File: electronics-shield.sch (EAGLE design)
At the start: 0 parts

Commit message: H-Bridge change from L298P to TLE9201S, better wiring
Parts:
- added C1, C11, C12, C13, C14, C19, C2, C20, C21, C22, C23, C3, C4, C6, C9: 100n, resistor:C-EUC0603K
- added C10: 1u, resistor:C-EUC0603K
- added C15: 4.7uF, resistor:C-EUC0603K
- added C16: 1uF, resistor:C-EUC0603K
- added C17: 100u, resistor:CPOL-EU153CLV-0807
- added C18: 22u, resistor:C-EUC0603K
- added C24: 0.1uF, rcl:C-EUC0603
- added C5: 4u7, resistor:C-EUC0603K
- added C7, C8: 20p, resistor:C-EUC0603K
- added D1, D10, D11, D12, D13, D14, D15, D16, D2, D3, D4, D5, D6, D7, D8, D9: SK38SMA, diode:DIODE-SOD123
- added D17: SMBJ5.0A-TR, diode:SUPPRESSOR-SMBJ
- added F1, F2, F3: SL125-33, polyfuse-smd_10:2920L050
- added IC1: MCP1703CB, linear:MCP1703CB
- added JP1: Listwa kołkowa 2.54mm prosta 1x2 (2pin), pinhead:PINHD-1X2
- added JP10: gniazdo IDC męskie 6pin proste, con-harting-ml:ML6
- added JP2, JP3, JP4: Listwa kołkowa 2.54mm prosta 1x3 (3pin), Synergiczne:PINHD-1X3STRAIGHT
- added JP5: Listwa stykowa 2.54mm prosta 2x20 (40-pin), wydłużona, RASPBERRY_PI_Bplus-eagle5:RASPBERRY_PI_B+_TPLACE
- added JP6: gniazdo IDC męskie 10pin proste, con-3m:2510-
- added JP7: gniazdo IDC męskie 8pin proste, Simplex-Connectors:2508-
- added JP8: Listwa zaciskowa rozłączalna 3.81mm 2pin kątowe 90° gniazdo, con-phoenix-381_l:MC2
- added JP9: Listwa zaciskowa rozłączalna 3.50mm 8pin kątowe 90° gniazdo, con-phoenix-350:1751303
- added PCB1, PCB2, PCB3: Moduł przetwornicy DC-DC Step-down 4.5..28V --- regulowane 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, Kell Ideas:MP1584
- added Q1: 8 MHz, crystal:CRYSTALHC49UP
- added Q2: MOSFET-PCHANNELSMD, User-Submitted:MOSFET-PCHANNELSMD
- added R1, R2, R3, R4: 10k, rcl:R-EU_R0603
- added R10: 100k, rcl:R-EU_R0603
- added R11, R13, R14, R5, R8, R9: 10k, resistor:R-EU_R0603
- added R12: 1k, resistor:R-EU_R0603
- added R6, R7: 4k7, resistor:R-EU_R0603
- added SJ1: Zworka cynowa, jumper:SJ2W
- added U1, U2, U3, U4: TLE9201SGAUMA1, Kell Ideas:TLE9201SGAUMA1
- added U5: STM32F051C8T, STM32F030:STM32F051C8T
- added U6, U7: SN74LVC4245APWR, Texas Instruments_By_element14_Batch_1:SN74LVC4245APWR
- added U8: 24LC256, SparkFun-IC-Memory:EEPROM-I2CSMD
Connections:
- new net +3V3: C10.1, C11.1, C19.1, C20.1, C24.1, C5.1, C6.1, C9.1, JP10.4, R5.2, R6.2, R7.2, R8.2, SJ1.2, U5PWR.VDD, U5PWR.VDDA, U6.VCCB_(3.3_V), U6.VCCB_(3.3_V)_2, U7.VCCB_(3.3_V), U7.VCCB_(3.3_V)_2, U8.VCC, U8.WP
- new net +5V: C1.1, C15.1, C2.1, C21.1, C22.1, C23.1, C3.1, C4.1, D17.C, IC1.VI, JP5.5V0@1, JP5.5V0@2, JP6-3.KL, JP7-2.KL, Q2.S, U1.VSO, U2.VSO, U3.VSO, U4.VSO, U6.(5_V)_VCCA, U7.(5_V)_VCCA
- new net +5V_RAW: F1.2, PCB1.VOUT+
- new net +7V/1: C13.1, F2.1, JP4.2, JP6-1.KL
- new net +7V/1_RAW: F2.2, PCB2.VOUT+
- new net +7V/2: C14.1, F3.2, JP2.2, JP3.2, JP6-2.KL
- new net +7V/2_RAW: F3.1, PCB3.VOUT+
- new net 3V3_RPI: JP5.3V3@1, SJ1.3
- new net 3V3_STABILIZED: C16.1, IC1.VO, SJ1.1
- new net 5V_NOT_TRIMMED: C12.1, F1.1, Q2.D
- new net BAT_MEAS: C18.1, R11.1, R12.2, U5PA.PA4
- new net BOOT0: R9.2, U5CTL.BOOT0
- new net D1-R3: D17.A, Q2.G, R10.2
- new net DATA_N: JP1.2, JP7-3.KL
- new net DATA_P: JP1.1, JP7-4.KL
- new net EN1: U1.PWM, U6.A1
- new net EN1_UC: U5PA.PA6, U6.B1
- new net EN2: U3.PWM, U6.A2
- new net EN2_UC: U5PA.PA7, U6.B2
- new net EN3: U2.PWM, U6.A3
- new net EN3_UC: U5PB.PB0, U6.B3
- new net EN4: U4.PWM, U6.A4
- new net EN4_UC: U5PB.PB1, U6.B4
- new net GND: C1.2, C10.2, C11.2, C12.2, C13.2, C14.2, C15.2, C16.2, C17.-, C18.2, C19.2, C2.2, C20.2, C21.2, C22.2, C23.2, C24.2, C3.2, C4.2, C5.2, C6.2, C7.1, C8.1, C9.2, D10.A, D11.A, D12.A, D13.A, D14.A, D15.A, D16.A, D9.A, IC1.GND, JP10.3, JP2.3, JP3.3, JP4.3, JP5.GND@1, JP5.GND@2, JP5.GND@3, JP5.GND@4, JP5.GND@5, JP5.GND@6, JP5.GND@7, JP5.GND@8, JP6-10.KL, JP6-9.KL, JP7-1.KL, JP7-8.KL, JP8.1.SK, PCB1.VIN-, PCB1.VOUT-, PCB2.VIN-, PCB2.VOUT-, PCB3.VIN-, PCB3.VOUT-, R1.1, R10.1, R12.1, R13.2, R14.2, R2.1, R3.1, R4.1, R9.1, U1.GND@1, U1.GND@2, U2.GND@1, U2.GND@2, U3.GND@1, U3.GND@2, U4.GND@1, U4.GND@2, U5PWR.VSS, U5PWR.VSSA, U6.GND, U6.GND_2, U6.GND_3, U7.GND, U7.GND_2, U7.GND_3, U8.A1, U8.A2, U8.VSS
- new net IN11: U1.DIR, U6.A5
- new net IN11_UC: U5PB.PB8, U6.B5
- new net IN12: U6.A6
- new net IN12_UC: U6.B6
- new net IN21: U3.DIR, U6.A7
- new net IN21_UC: U5PA.PA11, U6.B7
- new net IN22: U6.A8
- new net IN22_UC: U6.B8
- new net IN31: U2.DIR, U7.A1
- new net IN31_UC: U5PB.PB12, U7.B1
- new net IN32: U7.A2
- new net IN32_UC: U7.B2
- new net IN41: U4.DIR, U7.A3
- new net IN41_UC: U5PB.PB14, U7.B3
- new net IN42: U7.A4
- new net IN42_UC: U7.B4
- new net LED: U5PA.PA5
- new net MOT11: D16.C, D8.A, JP9-7.K, U1.OUT1
- new net MOT12: D15.C, D7.A, JP9-8.K, U1.OUT2
- new net MOT21: D14.C, D6.A, JP9-5.K, U3.OUT1
- new net MOT22: D13.C, D5.A, JP9-6.K, U3.OUT2
- new net MOT31: D12.C, D4.A, JP9-3.K, U2.OUT1
- new net MOT32: D11.C, D3.A, JP9-4.K, U2.OUT2
- new net MOT41: D10.C, D2.A, JP9-1.K, U4.OUT1
- new net MOT42: D1.A, D9.C, JP9-2.K, U4.OUT2
- new net N$1: R13.1, U6.DIR, U6.~OE
- new net N$2: R14.1, U7.DIR, U7.~OE
- new net N$3: U7.A8
- new net N$4: U7.B8
- new net N$8: JP10.6
- new net NRST: JP10.5, JP5.GPIO18, R8.1, U5CTL.NRST
- new net OSCILATOR_N: C7.2, Q1.2, U5CTL.PF0-OSC_IN
- new net OSCILATOR_P: C8.2, Q1.1, U5CTL.PF1-OSC_OUT
- new net RPI_CLK: JP5.GPIO11/SCLK, JP7-7.KL, U5PB.PB3
- new net RPI_MISO: JP5.GPIO09/MISO, JP7-5.KL, U5PB.PB4
- new net RPI_MOSI: JP5.GPIO10/MOSI, JP7-6.KL, U5PB.PB5
- new net RPI_RXD: JP5.RXD0/GPIO15, U5PB.PB6
- new net RPI_TXD: JP5.TXD0/GPIO14, U5PB.PB7
- new net SCL: JP5.GPIO03/SCL1, R7.1, U5PA.PF6, U8.SCL
- new net SCL_TX: JP6-5.KL, U5PB.PB10
- new net SDA: JP5.GPIO02/SDA1, R6.1, U5PA.PF7, U8.SDA
- new net SDA_RX: JP6-4.KL, U5PB.PB11
- new net SEN1: U5PA.PA0
- new net SEN2: U5PA.PA1
- new net SEN3: U5PA.PA2
- new net SEN4: U5PA.PA3
- new net SERVO1: JP2.1, JP6-6.KL, U7.A5
- new net SERVO1_UC: U5PA.PA8, U7.B5
- new net SERVO2: JP3.1, JP6-7.KL, U7.A6
- new net SERVO2_UC: U5PA.PA9, U7.B6
- new net SERVO3: JP4.1, JP6-8.KL, U7.A7
- new net SERVO3_UC: U5PA.PA10, U7.B7
- new net SPI1_NSS: JP5.!CE0!/GPIO08, R5.1, U5PA.PA15
- new net SWCLK: JP10.1, JP5.GEN6/GPIO25, U5PA.PA14-SWCLK
- new net SWDIO: JP10.2, JP5.GEN5/GPIO24, U5PA.PA13-SWDIO
- new net U5_DIS: R1.2, U1.DIS
- new net U6_DIS: R2.2, U2.DIS
- new net U7_DIS: R3.2, U3.DIS
- new net U8_DIS: R4.2, U4.DIS
- new net VCC: C17.+, D1.C, D2.C, D3.C, D4.C, D5.C, D6.C, D7.C, D8.C, JP8.2.SK, PCB1.VIN+, PCB2.VIN+, PCB3.VIN+, R11.2, U1.VS, U2.VS, U3.VS, U4.VS
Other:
- note added: "B to A"
- note added: "Battery Measurement"
- note added: "I2C2"
- note added: "MOTOR CONTROLLERS"
- note added: "Manipulator + USB"
- note added: "NC"
- note added: "Power Supply Raspberry 5V / 3A"
- note added: "Power Supply Servo 7V / 3 A"
- note added: "RPI HEADER"
- note added: "Second Servo PS 7V / 3 A"

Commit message: changed base for 7.c
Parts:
- removed C21, C22, C23: 100n, resistor:C-EUC0603K
- removed C24: 0.1uF, rcl:C-EUC0603
- removed JP10: gniazdo IDC męskie 6pin proste, con-harting-ml:ML6
- removed JP4: Listwa kołkowa 2.54mm prosta 1x3 (3pin), Synergiczne:PINHD-1X3STRAIGHT
- removed JP5: Listwa stykowa 2.54mm prosta 2x20 (40-pin), wydłużona, RASPBERRY_PI_Bplus-eagle5:RASPBERRY_PI_B+_TPLACE
- removed JP6: gniazdo IDC męskie 10pin proste, con-3m:2510-
- removed JP7: gniazdo IDC męskie 8pin proste, Simplex-Connectors:2508-
- removed JP8: Listwa zaciskowa rozłączalna 3.81mm 2pin kątowe 90° gniazdo, con-phoenix-381_l:MC2
- removed JP9: Listwa zaciskowa rozłączalna 3.50mm 8pin kątowe 90° gniazdo, con-phoenix-350:1751303
- removed PCB2, PCB3: Moduł przetwornicy DC-DC Step-down 4.5..28V --- regulowane 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, Kell Ideas:MP1584
- removed R14: 10k, resistor:R-EU_R0603
- removed U3, U4: TLE9201SGAUMA1, Kell Ideas:TLE9201SGAUMA1
- removed U5: STM32F051C8T, STM32F030:STM32F051C8T
- removed U6, U7: SN74LVC4245APWR, Texas Instruments_By_element14_Batch_1:SN74LVC4245APWR
- removed U8: 24LC256, SparkFun-IC-Memory:EEPROM-I2CSMD
- added $3_0_$_2018-08-14_21-12-08, $3_1_$_2018-08-14_21-12-08, $3_2_$_2018-08-14_21-12-08: Moduł przetwornicy DC-DC Step-down 4.5..28V --- regulowane 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, Kell Ideas:MP1584_MODULE
- added IC2, IC3, IC4: TLE9201SG, Kell Ideas:TLE9201SG
- added IC5: LINEAR_MCP1703CB, electronics-shield:LINEAR_MCP1703CB
- added J1: USB-MICRO-B, Kell Ideas:USB-MICRO-B
- added LED1, LED2, LED3, LED4, LED5: LEDCHIPLED_0603, audio amplifier example:LEDCHIPLED_0603
- added Q3: ON-SEMICONDUCTOR---NTZD3154NT1G_ON_SEMICONDUCTOR_NTZD3154NT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, electronics-shield:ON-SEMICONDUCTOR---NTZD3154NT1G_ON_SEMICONDUCTOR_NTZD3154NT1GON_SEMICONDUCTOR_NTZD3154NT1G_0_0
- added RN1, RN2: 1k, SparkFun-Resistors:1KOHM-ARRAY(4)-0805_ARV-1/10W-5%
- added SJ2: (no value), Kell Ideas:SOLDER_JUMPER
- added SV1: gniazdo IDC męskie 6pin proste, Kell Ideas:ML6
- added SV2: (no value), Kell Ideas:ML10
- added SV3: ML8, Kell Ideas:ML8
- added X1: CONNECTOR_PHOENIX_3.81, Kell Ideas:CONNECTOR_PHOENIX_3.81
- added X2: Listwa zaciskowa rozłączalna 3.50mm 8pin kątowe 90° gniazdo, Kell Ideas:CONNECTOR_PHOENIX
- added Y1: 8 MHz, Kell Ideas:CRYSTAL
- C1, C10, C11, C12, C13, C14, C15, C16, C18, C19, C2, C3, C4, C5, C6, C7, C8, C9: device resistor:C-EUC0603K -> Kell Ideas:CAPACITOR_SMD
- C17: device resistor:CPOL-EU153CLV-0807 -> Kell Ideas:CAPACITOR_POL_SMD
- C20: value 100n -> 0.1uF; device resistor:C-EUC0603K -> Kell Ideas:CAPACITOR_SMD
- D1, D10, D11, D12, D13, D14, D15, D16, D2, D3, D4, D5, D6, D7, D8, D9: device diode:DIODE-SOD123 -> Kell Ideas:DIODE_SMD
- D17: device diode:SUPPRESSOR-SMBJ -> Kell Ideas:SUPPRESSOR-SMBJ
- F1, F2, F3: device polyfuse-smd_10:2920L050 -> Kell Ideas:PPTCD
- IC1: value MCP1703CB -> TLE9201SG; device linear:MCP1703CB -> Kell Ideas:TLE9201SG
- JP1: value Listwa kołkowa 2.54mm prosta 1x2 (2pin) -> Listwa kołkowa 2.54mm prosta 1x3 (3pin); device pinhead:PINHD-1X2 -> Kell Ideas:PINHD-1X3_DNP
- JP2, JP3: device Synergiczne:PINHD-1X3STRAIGHT -> Kell Ideas:PINHD-1X3_DNP
- PCB1: value Moduł przetwornicy DC-DC Step-down 4.5..28V --- regulowane 0.8..20V MP1584 -> Listwa stykowa 2.54mm prosta 2x20 (40-pin), wydłużona; device Kell Ideas:MP1584 -> Kell Ideas:RASPBERRY_PI_B+_TPLACE
- Q1: value 8 MHz -> USER-SUBMITTED_MOSFET-PCHANNELSMD; device crystal:CRYSTALHC49UP -> electronics-shield:USER-SUBMITTED_MOSFET-PCHANNELSMD; LINK YIC 49SLMT 8.00MHZ 20PF 30PPM -> (none)
- Q2: value MOSFET-PCHANNELSMD -> ON-SEMICONDUCTOR---NTZD3154NT1G_ON_SEMICONDUCTOR_NTZD3154NT1GON_SEMICONDUCTOR_NTZD3154NT1G_0_0; device User-Submitted:MOSFET-PCHANNELSMD -> electronics-shield:ON-SEMICONDUCTOR---NTZD3154NT1G_ON_SEMICONDUCTOR_NTZD3154NT1GON_SEMICONDUCTOR_NTZD3154NT1G_0_0
- R1, R4: device rcl:R-EU_R0603 -> Kell Ideas:RESISTOR_SMD
- R10: value 100k -> 330; device rcl:R-EU_R0603 -> Kell Ideas:RESISTOR_SMD
- R11: value 10k -> 330; device resistor:R-EU_R0603 -> Kell Ideas:RESISTOR_SMD
- R12: value 1k -> 200; device resistor:R-EU_R0603 -> Kell Ideas:RESISTOR_SMD
- R13: value 10k -> 200; device resistor:R-EU_R0603 -> Kell Ideas:RESISTOR_SMD
- R2, R3: value 10k -> 4k7; device rcl:R-EU_R0603 -> Kell Ideas:RESISTOR_SMD
- R5: device resistor:R-EU_R0603 -> Kell Ideas:RESISTOR_SMD
- R6: value 4k7 -> 100k; device resistor:R-EU_R0603 -> Kell Ideas:RESISTOR_SMD
- R7: value 4k7 -> 10k; device resistor:R-EU_R0603 -> Kell Ideas:RESISTOR_SMD
- R8: value 10k -> 1k; device resistor:R-EU_R0603 -> Kell Ideas:RESISTOR_SMD
- R9: value 10k -> 1.5k; device resistor:R-EU_R0603 -> Kell Ideas:RESISTOR_SMD
- SJ1: value Zworka cynowa -> (none); device jumper:SJ2W -> Kell Ideas:SOLDER_JUMPER
- U1: value TLE9201SGAUMA1 -> STM32F0XX8T; device Kell Ideas:TLE9201SGAUMA1 -> Kell Ideas:STM32F0XX8T
- U2: value TLE9201SGAUMA1 -> EEPROM-I2C; device Kell Ideas:TLE9201SGAUMA1 -> Kell Ideas:EEPROM-I2C
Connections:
- removed net EN1_UC: U5PA.PA6, U6.B1
- removed net EN2_UC: U5PA.PA7, U6.B2
- removed net EN3_UC: U5PB.PB0, U6.B3
- removed net EN4_UC: U5PB.PB1, U6.B4
- removed net IN11_UC: U5PB.PB8, U6.B5
- removed net IN12: U6.A6
- removed net IN12_UC: U6.B6
- removed net IN21_UC: U5PA.PA11, U6.B7
- removed net IN22: U6.A8
- removed net IN22_UC: U6.B8
- removed net IN31_UC: U5PB.PB12, U7.B1
- removed net IN32: U7.A2
- removed net IN32_UC: U7.B2
- removed net IN41_UC: U5PB.PB14, U7.B3
- removed net IN42: U7.A4
- removed net IN42_UC: U7.B4
- removed net U5_DIS: R1.2, U1.DIS
- removed net U6_DIS: R2.2, U2.DIS
- removed net U7_DIS: R3.2, U3.DIS
- removed net U8_DIS: R4.2, U4.DIS
- new net N$14: Q2B.S2, RN2C.1
- new net N$16: Q2B.D2, RN2D.1
- new net N$5: LED5.C, R13.1
- new net SO1-SI3: IC1.SO, IC3.SI
- new net SO2-SI4: IC2.SO, IC4.SI
- new net SO3-SI2: IC2.SI, IC3.SO
- new net TLE_NSS: IC1.CS_N, IC2.CS_N, IC3.CS_N, IC4.CS_N, U1PB.PB2
- net +3V3: now also C1.1, C2.1, C3.1, C4.1, IC1.VSO, IC2.VSO, IC3.VSO, IC4.VSO, LED5.A, Q2A.G1, Q2B.G2, Q3A.G1, Q3B.G2, R1.2, R2.2, R3.2, R4.2, RN1A.2, RN1C.2, RN2A.2, RN2C.2, SJ1.1, SJ2.1, SV1.4, U1PWR.VDD, U1PWR.VDDA, U2.VCC, U2.WP; no longer C19.1, C24.1, JP10.4, R5.2, R6.2, R7.2, R8.2, SJ1.2, U5PWR.VDD, U5PWR.VDDA, U6.VCCB_(3.3_V), U6.VCCB_(3.3_V)_2, U7.VCCB_(3.3_V), U7.VCCB_(3.3_V)_2, U8.VCC, U8.WP
- net +5V: now also C19.1, IC5.VI, LED4.A, PCB1.5V0@1, PCB1.5V0@2, Q1.S, RN1B.2, RN1D.2, RN2B.2, RN2D.2, SV2.3, SV3.P$2; no longer C1.1, C2.1, C21.1, C22.1, C23.1, C3.1, C4.1, IC1.VI, JP5.5V0@1, JP5.5V0@2, JP6-3.KL, JP7-2.KL, Q2.S, U1.VSO, U2.VSO, U3.VSO, U4.VSO, U6.(5_V)_VCCA, U7.(5_V)_VCCA
- net +5V_RAW: now also $3_0_$_2018-08-14_21-12-08.VOUT+; no longer PCB1.VOUT+
- net +7V/1: now also JP3.2, LED2.A, SV2.1; no longer JP4.2, JP6-1.KL
- net +7V/1_RAW: now also $3_1_$_2018-08-14_21-12-08.VOUT+; no longer PCB2.VOUT+
- net +7V/2: now also JP1.2, LED3.A, SV2.2; no longer JP3.2, JP6-2.KL
- net +7V/2_RAW: now also $3_2_$_2018-08-14_21-12-08.VOUT+; no longer PCB3.VOUT+
- net 3V3_RPI: now also PCB1.3V3@1, SJ2.2; no longer JP5.3V3@1, SJ1.3
- net 3V3_STABILIZED: now also IC5.VO, SJ1.2; no longer IC1.VO, SJ1.1
- net 5V_NOT_TRIMMED: now also Q1.D; no longer Q2.D
- net BAT_MEAS: now also R7.1, R8.2, U1PA.PA4; no longer R11.1, R12.2, U5PA.PA4
- net BOOT0: now also R5.2, U1CTL.BOOT0; no longer R9.2, U5CTL.BOOT0
- net D1-R3: now also Q1.G, R6.2; no longer Q2.G, R10.2
- net DATA_N: now also J1.D-, SV3.P$3; no longer JP1.2, JP7-3.KL
- net DATA_P: now also J1.D+, SV3.P$4; no longer JP1.1, JP7-4.KL
- net EN1: now also IC1.PWM, U1PA.PA6; no longer U1.PWM, U6.A1
- net EN2: now also IC3.PWM, U1PA.PA7; no longer U3.PWM, U6.A2
- net EN3: now also IC2.PWM, U1PB.PB0; no longer U2.PWM, U6.A3
- net EN4: now also IC4.PWM, U1PB.PB1; no longer U4.PWM, U6.A4
- net GND: now also $3_0_$_2018-08-14_21-12-08.VIN-, $3_0_$_2018-08-14_21-12-08.VOUT-, $3_1_$_2018-08-14_21-12-08.VIN-, $3_1_$_2018-08-14_21-12-08.VOUT-, $3_2_$_2018-08-14_21-12-08.VIN-, $3_2_$_2018-08-14_21-12-08.VOUT-, IC1.DIS, IC1.GND@1, IC1.GND@2, IC2.DIS, IC2.GND@1, IC2.GND@2, IC3.DIS, IC3.GND@1, IC3.GND@2, IC4.DIS, IC4.GND@1, IC4.GND@2, IC5.GND, J1.GND, J1.SHEILD, JP1.3, PCB1.GND@1, PCB1.GND@2, PCB1.GND@3, PCB1.GND@4, PCB1.GND@5, PCB1.GND@6, PCB1.GND@7, PCB1.GND@8, R10.2, R11.2, R12.2, R5.1, R6.1, R8.1, R9.2, SV1.3, SV2.10, SV2.9, SV3.P$1, SV3.P$8, U1PWR.VSS, U1PWR.VSSA, U2.A1, U2.A2, U2.VSS, X1G$1.K; no longer C21.2, C22.2, C23.2, C24.2, IC1.GND, JP10.3, JP4.3, JP5.GND@1, JP5.GND@2, JP5.GND@3, JP5.GND@4, JP5.GND@5, JP5.GND@6, JP5.GND@7, JP5.GND@8, JP6-10.KL, JP6-9.KL, JP7-1.KL, JP7-8.KL, JP8.1.SK, PCB1.VIN-, PCB1.VOUT-, PCB2.VIN-, PCB2.VOUT-, PCB3.VIN-, PCB3.VOUT-, R1.1, R10.1, R12.1, R14.2, R2.1, R3.1, R4.1, R9.1, U1.GND@1, U1.GND@2, U2.GND@1, U2.GND@2, U3.GND@1, U3.GND@2, U4.GND@1, U4.GND@2, U5PWR.VSS, U5PWR.VSSA, U6.GND, U6.GND_2, U6.GND_3, U7.GND, U7.GND_2, U7.GND_3, U8.A1, U8.A2, U8.VSS
- net IN11: now also IC1.DIR, U1PB.PB8; no longer U1.DIR, U6.A5
- net IN21: now also IC3.DIR, U1PA.PA11; no longer U3.DIR, U6.A7
- net IN31: now also IC2.DIR, U1PB.PB12; no longer U2.DIR, U7.A1
- net IN41: now also IC4.DIR, U1PB.PB14; no longer U4.DIR, U7.A3
- net LED: now also U1PA.PA5; no longer U5PA.PA5
- net MOT11: now also IC1.OUT1, X2-7.K; no longer JP9-7.K, U1.OUT1
- net MOT12: now also IC1.OUT2, X2-8.K; no longer JP9-8.K, U1.OUT2
- net MOT21: now also IC3.OUT1, X2-5.K; no longer JP9-5.K, U3.OUT1
- net MOT22: now also IC3.OUT2, X2-6.K; no longer JP9-6.K, U3.OUT2
- net MOT31: now also IC2.OUT1, X2-3.K; no longer JP9-3.K, U2.OUT1
- net MOT32: now also IC2.OUT2, X2-4.K; no longer JP9-4.K, U2.OUT2
- net MOT41: now also IC4.OUT1, X2-1.K; no longer JP9-1.K, U4.OUT1
- net MOT42: now also IC4.OUT2, X2-2.K; no longer JP9-2.K, U4.OUT2
- net N$1: now also LED1.C, R9.1; no longer R13.1, U6.DIR, U6.~OE
- net N$2: now also LED2.C, R10.1; no longer R14.1, U7.DIR, U7.~OE
- net N$3: now also LED3.C, R11.1; no longer U7.A8
- net N$4: now also LED4.C, R12.1; no longer U7.B8
- net N$8: now also SV1.6; no longer JP10.6
- net NRST: now also PCB1.GPIO18, R4.1, SV1.5, U1CTL.NRST; no longer JP10.5, JP5.GPIO18, R8.1, U5CTL.NRST
- net OSCILATOR_N: now also U1CTL.PF0-OSC_IN, Y1.2; no longer Q1.2, U5CTL.PF0-OSC_IN
- net OSCILATOR_P: now also U1CTL.PF1-OSC_OUT, Y1.1; no longer Q1.1, U5CTL.PF1-OSC_OUT
- net RPI_CLK: now also IC1.SCK, IC2.SCK, IC3.SCK, IC4.SCK, PCB1.GPIO11/SCLK, SV3.P$7, U1PB.PB3; no longer JP5.GPIO11/SCLK, JP7-7.KL, U5PB.PB3
- net RPI_MISO: now also IC4.SO, PCB1.GPIO09/MISO, SV3.P$5, U1PB.PB4; no longer JP5.GPIO09/MISO, JP7-5.KL, U5PB.PB4
- net RPI_MOSI: now also IC1.SI, PCB1.GPIO10/MOSI, SV3.P$6, U1PB.PB5; no longer JP5.GPIO10/MOSI, JP7-6.KL, U5PB.PB5
- net RPI_RXD: now also PCB1.RXD0/GPIO15, U1PB.PB6; no longer JP5.RXD0/GPIO15, U5PB.PB6
- net RPI_TXD: now also PCB1.TXD0/GPIO14, U1PB.PB7; no longer JP5.TXD0/GPIO14, U5PB.PB7
- net SCL: now also PCB1.GPIO03/SCL1, R3.1, U1PA.PF6, U2.SCL; no longer JP5.GPIO03/SCL1, R7.1, U5PA.PF6, U8.SCL
- net SCL_TX: now also SV2.5, U1PB.PB10; no longer JP6-5.KL, U5PB.PB10
- net SDA: now also PCB1.GPIO02/SDA1, R2.1, U1PA.PF7, U2.SDA; no longer JP5.GPIO02/SDA1, R6.1, U5PA.PF7, U8.SDA
- net SDA_RX: now also SV2.4, U1PB.PB11; no longer JP6-4.KL, U5PB.PB11
- net SEN1: now also U1PA.PA0; no longer U5PA.PA0
- net SEN2: now also U1PA.PA1; no longer U5PA.PA1
- net SEN3: now also U1PA.PA2; no longer U5PA.PA2
- net SEN4: now also U1PA.PA3; no longer U5PA.PA3
- net SERVO1: now also JP1.1, Q3B.D2, RN1D.1, SV2.6; no longer JP2.1, JP6-6.KL, U7.A5
- net SERVO1_UC: now also Q3B.S2, RN1C.1, U1PA.PA8; no longer U5PA.PA8, U7.B5
- net SERVO2: now also JP2.1, Q3A.D1, RN1B.1, SV2.7; no longer JP3.1, JP6-7.KL, U7.A6
- net SERVO2_UC: now also Q3A.S1, RN1A.1, U1PA.PA9; no longer U5PA.PA9, U7.B6
- net SERVO3: now also JP3.1, Q2A.D1, RN2B.1, SV2.8; no longer JP4.1, JP6-8.KL, U7.A7
- net SERVO3_UC: now also Q2A.S1, RN2A.1, U1PA.PA10; no longer U5PA.PA10, U7.B7
- net SPI1_NSS: now also PCB1.!CE0!/GPIO08, R1.1, U1PA.PA15; no longer JP5.!CE0!/GPIO08, R5.1, U5PA.PA15
- net SWCLK: now also PCB1.GEN6/GPIO25, SV1.1, U1PA.PA14-SWCLK; no longer JP10.1, JP5.GEN6/GPIO25, U5PA.PA14-SWCLK
- net SWDIO: now also PCB1.GEN5/GPIO24, SV1.2, U1PA.PA13-SWDIO; no longer JP10.2, JP5.GEN5/GPIO24, U5PA.PA13-SWDIO
- net VCC: now also $3_0_$_2018-08-14_21-12-08.VIN+, $3_1_$_2018-08-14_21-12-08.VIN+, $3_2_$_2018-08-14_21-12-08.VIN+, IC1.VS, IC2.VS, IC3.VS, IC4.VS, LED1.A, R7.2, X1G$2.K; no longer JP8.2.SK, PCB1.VIN+, PCB2.VIN+, PCB3.VIN+, R11.2, U1.VS, U2.VS, U3.VS, U4.VS
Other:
- note removed: "B to A"

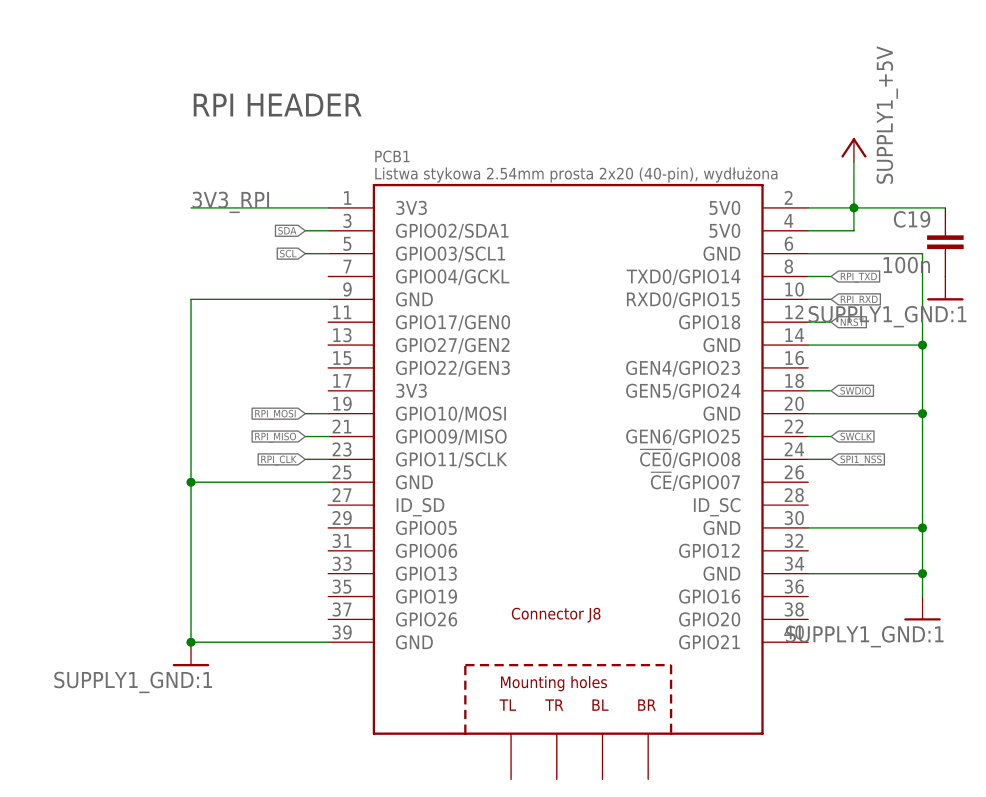
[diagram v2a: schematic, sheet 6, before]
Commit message: Added place to solder additional DC/DC converter, removed PTC from serwo power lines
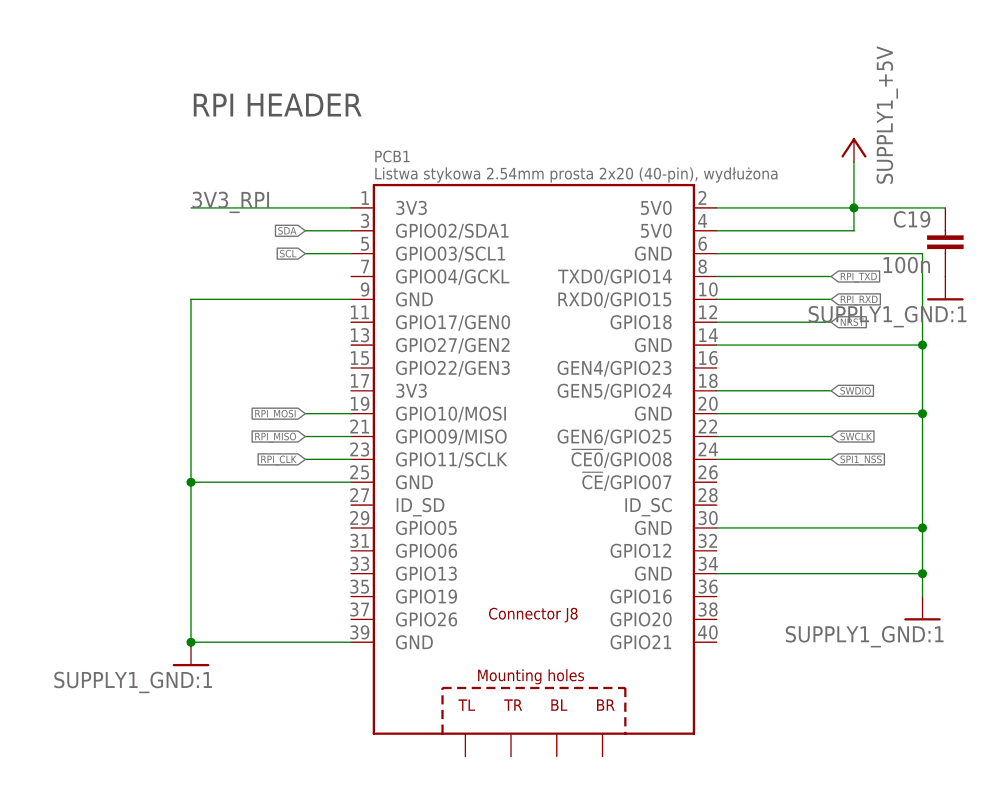
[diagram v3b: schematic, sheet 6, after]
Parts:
- removed C13, C14: 100n, Kell Ideas:CAPACITOR_SMD
- removed F2, F3: SL125-33, Kell Ideas:PPTCD
- removed LED2, LED3: LEDCHIPLED_0603, audio amplifier example:LEDCHIPLED_0603
- removed R10, R11: 330, Kell Ideas:RESISTOR_SMD
- added JP5: (no value), pinhead:PINHD-1X1
- C1, C10, C11, C12, C15, C16, C18, C19, C2, C20, C3, C4, C5, C6, C7, C8, C9: device Kell Ideas:CAPACITOR_SMD -> Kell Ideas:CAPACITOR_SMD_0603
- R1, R12, R13, R2, R3, R4, R5, R6, R7, R8, R9: device Kell Ideas:RESISTOR_SMD -> Kell Ideas:RESISTOR_SMD_0603
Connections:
- removed net +7V/1_RAW: $3_1_$_2018-08-14_21-12-08.VOUT+, F2.2
- removed net +7V/2_RAW: $3_2_$_2018-08-14_21-12-08.VOUT+, F3.1
- removed net N$2: LED2.C, R10.1
- removed net N$3: LED3.C, R11.1
- new net +5V/2: JP1.2, JP5.1, SV2.3
- net +5V: no longer SV2.3
- net +7V/1: now also $3_1_$_2018-08-14_21-12-08.VOUT+; no longer C13.1, F2.1, LED2.A
- net +7V/2: now also $3_2_$_2018-08-14_21-12-08.VOUT+; no longer C14.1, F3.2, JP1.2, LED3.A
- net GND: no longer C13.2, C14.2, R10.2, R11.2
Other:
- moved on the sheet: PCB1

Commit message: 7C+ release
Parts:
- JP5: value (none) -> Listwa kołkowa 2.54mm prosta 1x1 (1pin)
- Q2, Q3: value ON-SEMICONDUCTOR---NTZD3154NT1G_ON_SEMICONDUCTOR_NTZD3154NT1GON_SEMICONDUCTOR_NTZD3154NT1G_0_0 -> NTZD3154NT1G
- SV1: value gniazdo IDC męskie 6pin proste -> Gniazdo IDC męskie 6pin proste
- SV2: value (none) -> Gniazdo IDC męskie 10pin proste
- SV3: value ML8 -> Gniazdo IDC męskie 8pin proste
- renumbered $3_0_$_2018-08-14_21-12-08 to IC6, $3_1_$_2018-08-14_21-12-08 to IC7, $3_2_$_2018-08-14_21-12-08 to IC8
